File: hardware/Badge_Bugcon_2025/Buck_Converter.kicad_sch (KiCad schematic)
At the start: 40 parts, among them U7 EA3059

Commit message: feat(Hw):Update_Schematic_And_Floorplan
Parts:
- R39: footprint Resistor_SMD:R_0603_1608Metric -> Resistor_SMD:R_0402_1005Metric; LCSC# C253328 -> C2906860
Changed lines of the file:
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@@
 			)
 		)
-		(property "Footprint" "Resistor_SMD:R_0603_1608Metric"
+		(property "Footprint" "Resistor_SMD:R_0402_1005Metric"
 			(at 209.55 66.04 0)
 			(effects
@@
 			)
 		)
-		(property "LCSC#" "C253328"
+		(property "LCSC#" "C2906860"
 			(at 209.55 66.04 90)
 			(effects

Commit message: feat(Hw):Update_Schematic
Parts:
- R39: value 100 -> 330; LCSC# C2906860 -> C105875
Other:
- note added: "0V9 OUT"
- note added: "1V8 OUT"
- note added: "1V8 OUT(VCC_DDR)"
- note added: "3V3 OUT"
- note added: "BUCK"
- note removed: "BUCK (1.2V, 1.8V, 3.3V)"
- moved on the sheet: C10, C11, C12, C13, C14, C15, C16, C17, C58, C59, C61, C7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

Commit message: feat(Hw):Update_Schematic
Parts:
- R5: LCSC# (none) -> C2909311
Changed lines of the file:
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@@
+			)
+		)
+		(property "LCSC#" "C2909311"
+			(at 167.64 57.15 90)
+			(effects
+				(font
+					(size 1.27 1.27)
+				)
+				(hide yes)
 			)
 		)

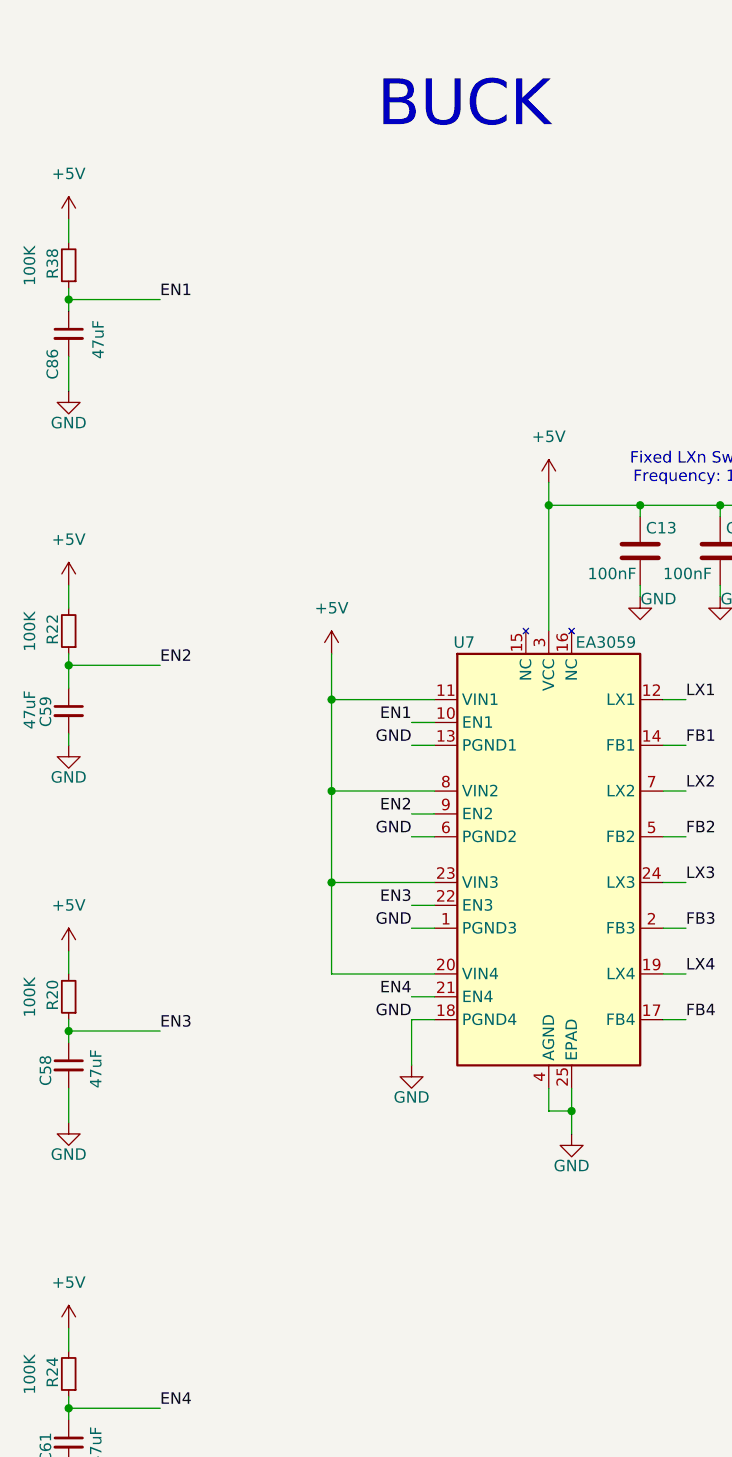
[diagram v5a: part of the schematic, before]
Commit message: feat(Hw):Update_Schematic_And_Floorplan
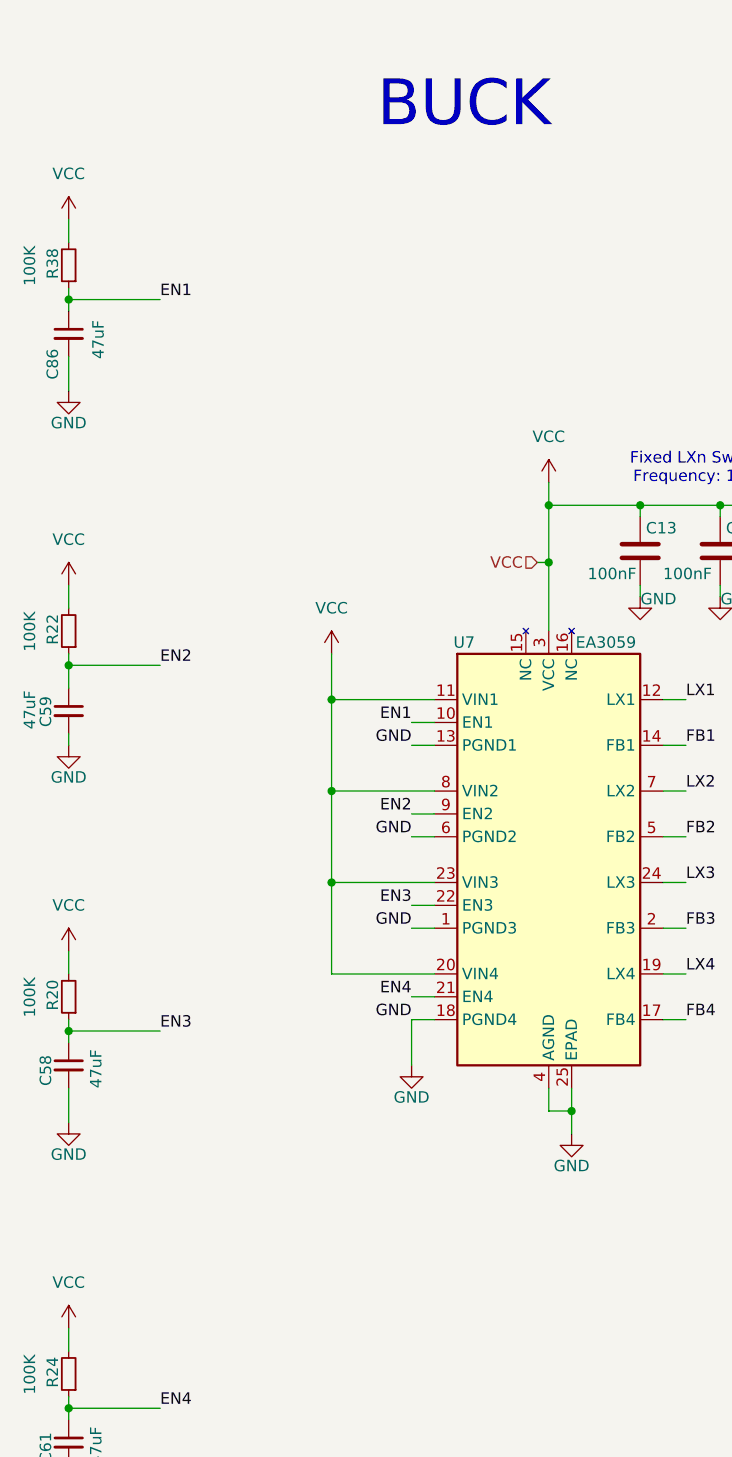
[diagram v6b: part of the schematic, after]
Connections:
- net +5V renamed VCC

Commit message: feat(Hw):Update_BOM_And_Labels
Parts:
- R41, R42, R43: LCSC# C445802 -> C2907181
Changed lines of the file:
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@@
 			)
 		)
-		(property "LCSC#" "C445802"
+		(property "LCSC#" "C2907181"
 			(at 201.93 116.84 90)
 			(effects
@@
 			)
 		)
-		(property "LCSC#" "C445802"
+		(property "LCSC#" "C2907181"
 			(at 270.51 43.18 90)
 			(effects
@@
 			)
 		)
-		(property "LCSC#" "C445802"
+		(property "LCSC#" "C2907181"
 			(at 270.51 116.84 90)
 			(effects
